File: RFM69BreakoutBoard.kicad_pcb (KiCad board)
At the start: 2 copper layers, 25.4 x 25.4 mm, 15 parts, among them P1 BB Holes, P10 TST, P11 TST, P12 TST, P8 TST, P9 TST, U1 MCP1703, U2 74HCT123, U3 RFM69HW

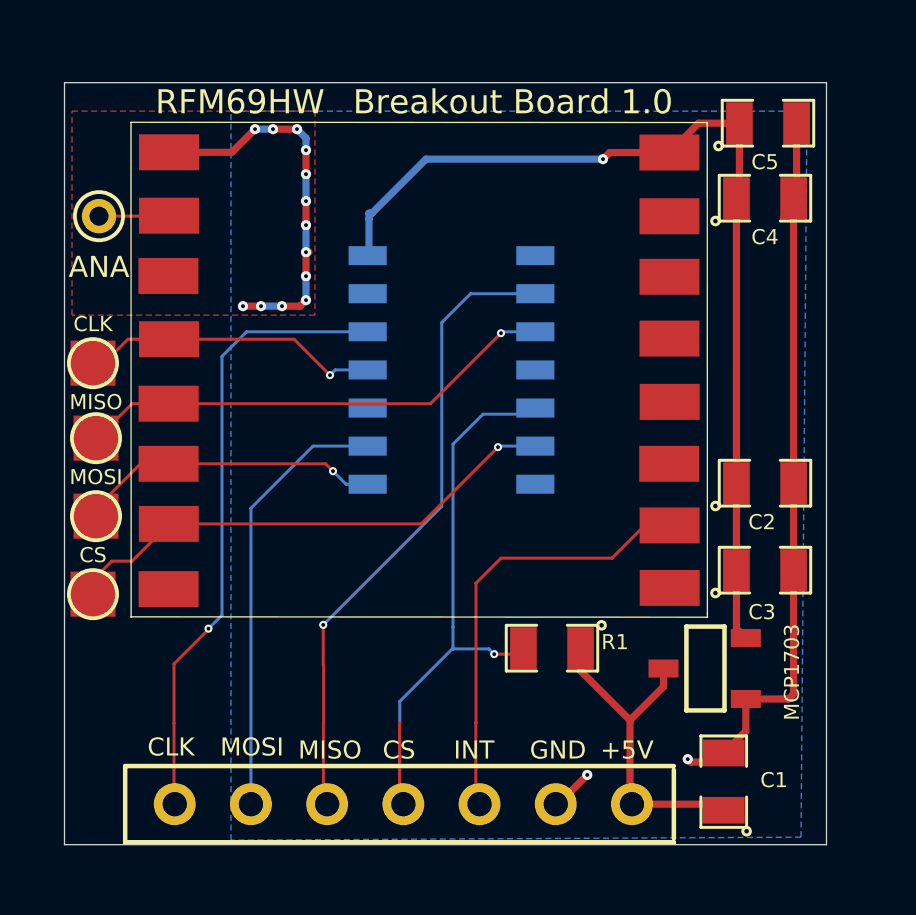
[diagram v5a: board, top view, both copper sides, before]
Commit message: updated PCB layout after correcting for freeDFM.com errors
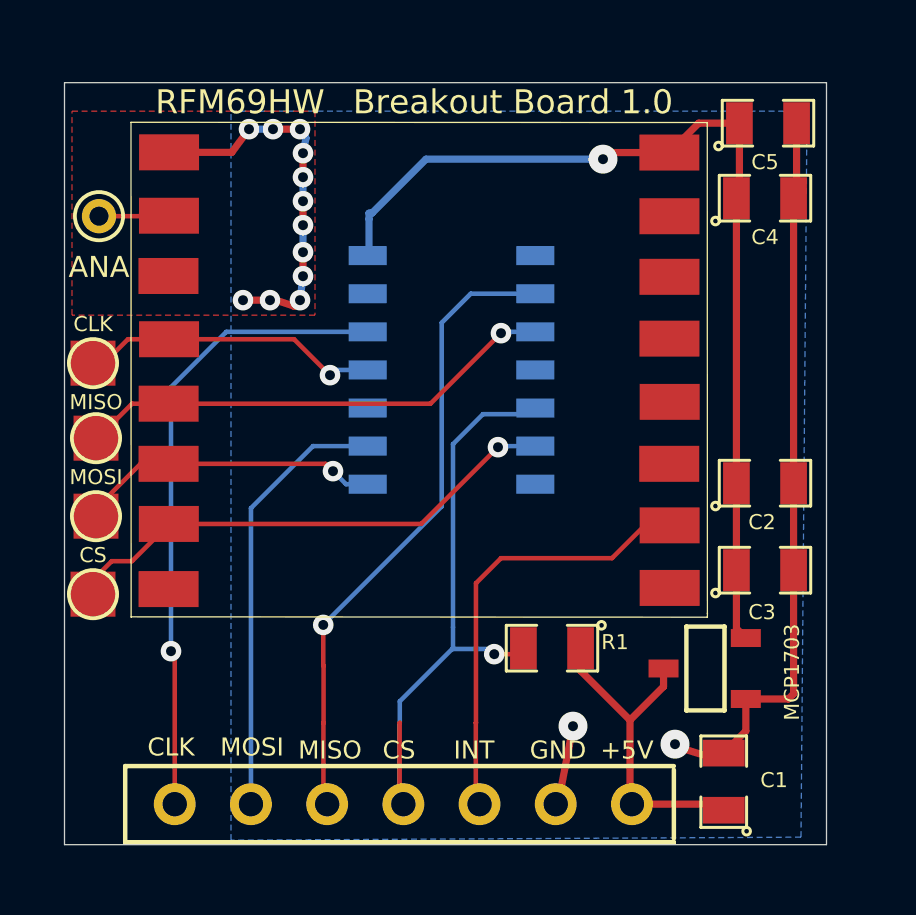
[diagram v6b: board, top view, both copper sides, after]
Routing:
- net GND: track 38.3 -> 40.0 mm, vias 15 -> 14
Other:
- net class Default: trace_width 0.1 -> 0.1524; via_dia 0.27 -> 0.6858; via_drill 0.13 -> 0.3302
- net class POWER: trace_width 0.24 -> 0.254; via_dia 0.34 -> 0.9652; via_drill 0.2 -> 0.4572
- rule trace_min: 0.1 -> 0.1524
- rule via_min_drill: 0.13 -> 0.3302
- rule via_min_size: 0.27 -> 0.6858
